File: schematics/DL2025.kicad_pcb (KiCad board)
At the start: 2 copper layers, 95.5 x 45.3 mm, 6 parts, among them U1 ATmega328PB-A, U2 DS18B20, U3 BMP280, U4 SC16IS750xPW, U8 CC56-12GWA, U9 AMS1117-3.3

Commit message: updated PCB schematic
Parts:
- removed U4: SC16IS750xPW, Package_SO:TSSOP-24_4.4x7.8mm_P0.65mm
- added C1: 100n, Capacitor_THT:C_Radial_D4.0mm_H5.0mm_P1.50mm, F.Cu at (132.6, 31.2)
- added C2: 100n, Capacitor_THT:C_Radial_D4.0mm_H5.0mm_P1.50mm, F.Cu at (114.8, 28.4)
- added C3: 100n, Capacitor_THT:C_Radial_D4.0mm_H5.0mm_P1.50mm, F.Cu at (144.9, 57.0)
- added C4: 100n, Capacitor_THT:C_Radial_D4.0mm_H5.0mm_P1.50mm, F.Cu at (113.7, 52.3)
- added C5: 100n, Capacitor_THT:C_Radial_D4.0mm_H5.0mm_P1.50mm, F.Cu at (110.3, 28.4)
- added C6: 100n, Capacitor_THT:C_Radial_D4.0mm_H5.0mm_P1.50mm, F.Cu at (129.8, 40.2)
- added J1: Micro_SD_Card, Connector_PinHeader_1.00mm:PinHeader_1x09_P1.00mm_Horizontal, F.Cu at (149.1, 54.1)
- added R1: 4.7K, Resistor_THT:R_Axial_DIN0207_L6.3mm_D2.5mm_P2.54mm_Vertical, F.Cu at (139.3, 31.0)
- added R2: 4.7K, Resistor_THT:R_Axial_DIN0207_L6.3mm_D2.5mm_P2.54mm_Vertical, F.Cu at (138.7, 25.3)
- added U5: FT232RL, Package_SO:SSOP-28_5.3x10.2mm_P0.65mm, F.Cu at (122.8, 38.8)
- moved U9 0.68 mm to (122.6, 26.2)
- moved U1 0.26 mm to (124.7, 55.3)
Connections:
- U1 pad 4: +5V -> Net-(U1-VCC)
- U3 pad 3: Net-(U1-PC4) -> Net-(U3-SDI)
- U3 pad 4: Net-(U1-PC5) -> Net-(U3-SCK)
- U9 pad 3: +5V -> Net-(U9-VI)
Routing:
- net Net-(U9-VO): track 6.36 -> 134.5 mm, vias 0 -> 1
- net GND: track 147.2 -> 24.3 mm, vias 0 -> 11
- net Net-(J1-DAT3/CD): track 0.00 -> 69.8 mm
- net Net-(U1-PC0): track 109.4 -> 47.3 mm
- net Net-(U1-PE3): track 106.9 -> 52.6 mm
- net Net-(U1-PE2): track 124.4 -> 72.1 mm
- net Net-(J1-DAT0): track 67.2 -> 25.4 mm
- net Net-(J1-CMD): track 0.00 -> 30.5 mm
- net Net-(U1-PE1): track 150.8 -> 123.5 mm
- net Net-(U1-PC1): track 64.0 -> 41.7 mm
- net Net-(J1-CLK): track 0.00 -> 20.6 mm
- net Net-(U1-VCC): track 0.00 -> 10.8 mm
- net Net-(U3-SDI): track 0.00 -> 9.30 mm
- net Net-(U1-PE0): track 116.9 -> 108.1 mm
- net Net-(U1-PB0): track 152.1 -> 143.4 mm
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- added copper zone on B.Cu, net GND
- added copper zone on F.Cu, net GND

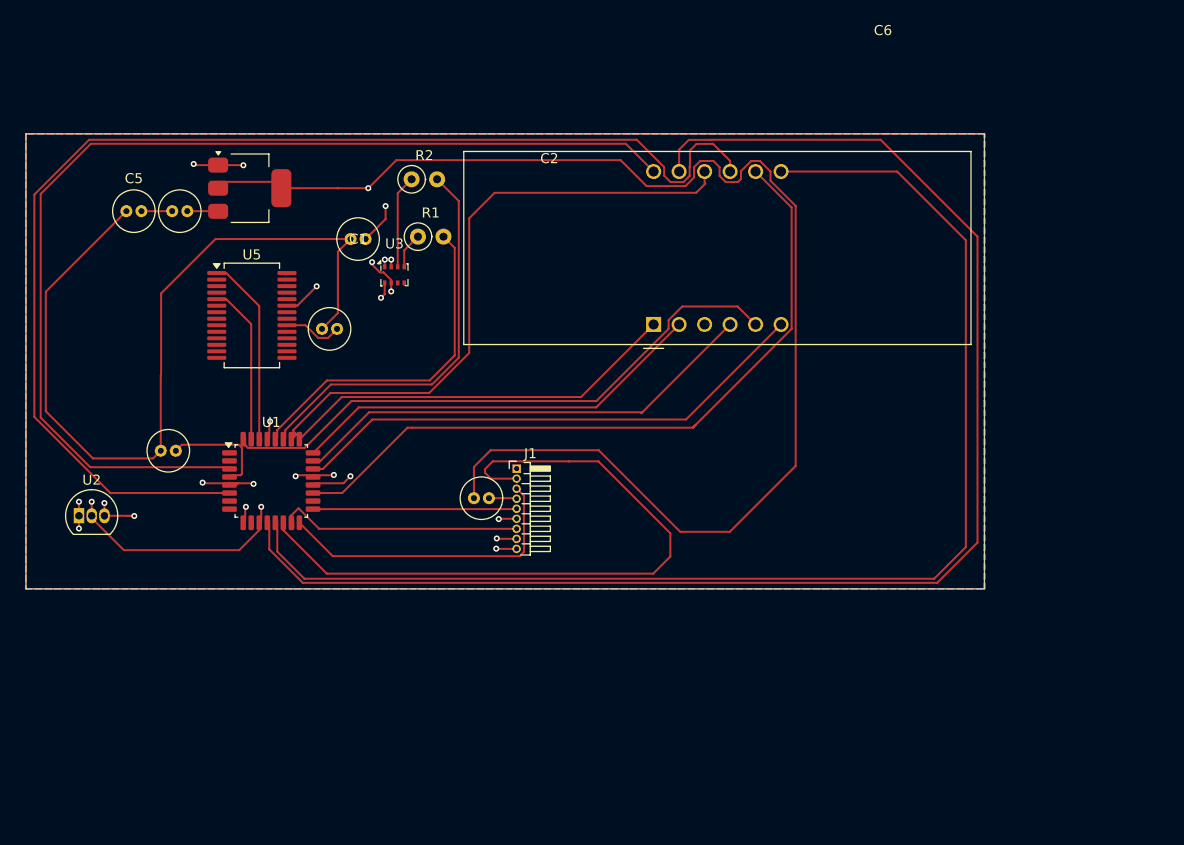
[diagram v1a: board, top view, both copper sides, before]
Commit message: updated schematics
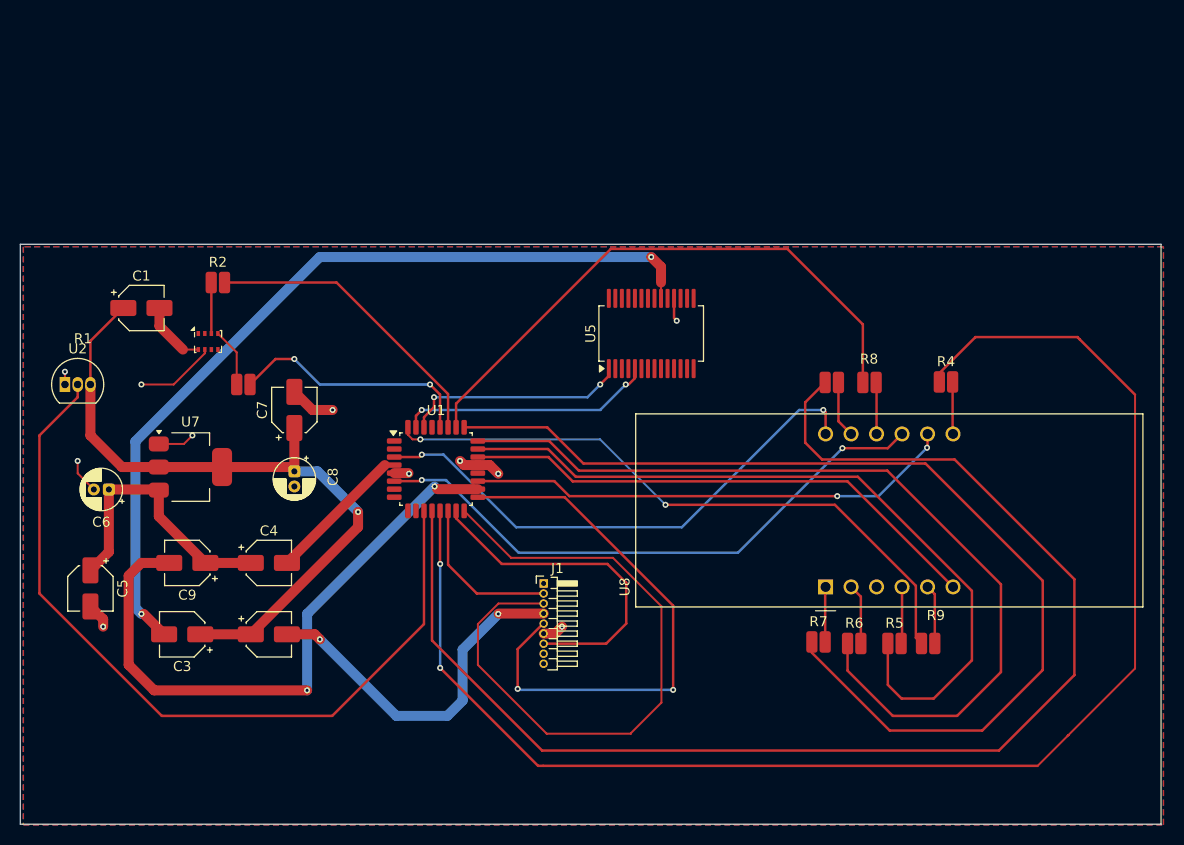
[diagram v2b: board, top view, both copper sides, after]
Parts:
- removed U9: AMS1117-3.3, Package_TO_SOT_SMD:SOT-223-3_TabPin2
- added C7: 100n, Capacitor_SMD:CP_Elec_4x3, F.Cu at (127.0, 48.3)
- added C8: 10u, Capacitor_THT:CP_Radial_D4.0mm_P1.50mm, F.Cu at (127.0, 54.4)
- added C9: 100n, Capacitor_SMD:CP_Elec_4x3, F.Cu at (116.3, 63.5)
- added R3: 220, Resistor_SMD:R_0508_1220Metric_Pad1.12x2.15mm_HandSolder, F.Cu at (180.6, 45.5)
- added R4: 220, Resistor_SMD:R_0508_1220Metric_Pad1.12x2.15mm_HandSolder, F.Cu at (191.9, 45.5)
- added R5: 220, Resistor_SMD:R_0508_1220Metric_Pad1.12x2.15mm_HandSolder, F.Cu at (186.8, 71.5)
- added R6: 220, Resistor_SMD:R_0508_1220Metric_Pad1.12x2.15mm_HandSolder, F.Cu at (182.8, 71.5)
- added R7: 220, Resistor_SMD:R_0508_1220Metric_Pad1.12x2.15mm_HandSolder, F.Cu at (179.2, 71.4)
- added R8: 220, Resistor_SMD:R_0508_1220Metric_Pad1.12x2.15mm_HandSolder, F.Cu at (184.3, 45.5)
- added R9: 220, Resistor_SMD:R_0508_1220Metric_Pad1.12x2.15mm_HandSolder, F.Cu at (190.2, 71.5)
- added U7: AMS1117-3.3, Package_TO_SOT_SMD:SOT-223-3_TabPin2, F.Cu at (116.6, 53.9)
- C1, C2, C3, C4, C5: footprint Capacitor_THT:C_Radial_D4.0mm_H5.0mm_P1.50mm -> Capacitor_SMD:CP_Elec_4x3
- C6: value 100n -> 10u; footprint Capacitor_THT:C_Radial_D4.0mm_H5.0mm_P1.50mm -> Capacitor_THT:CP_Radial_D4.0mm_P1.50mm
- R1, R2: footprint Resistor_THT:R_Axial_DIN0207_L6.3mm_D2.5mm_P2.54mm_Vertical -> Resistor_SMD:R_0508_1220Metric_Pad1.12x2.15mm_HandSolder
- moved C2 43.2 mm to (124.5, 70.6)
- moved U5 39.8 mm to (162.6, 40.6), turned to 90 degrees
- moved C5 37.8 mm to (106.7, 66.0), turned to -90 degrees
- moved C3 32.1 mm to (115.8, 70.6), turned to 180 degrees
- moved U8 31.3 mm to (179.9, 65.9)
- moved C6 26.6 mm to (108.5, 56.2), turned to 180 degrees
- moved R1 22.8 mm to (121.9, 45.7)
- moved C1 21.9 mm to (111.8, 38.1)
- moved R2 21.9 mm to (119.4, 35.6)
- moved U3 19.7 mm to (118.4, 41.4)
- moved U1 16.5 mm to (141.1, 54.1)
- moved C4 15.5 mm to (124.5, 63.5)
- moved U2 13.2 mm to (104.1, 45.7)
- moved J1 11.8 mm to (151.8, 65.5)
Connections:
- C1 pad 1: +5V -> Net-(U2-V_{DD})
- C2 pad 1: Net-(U7-VI) -> Net-(U2-V_{DD})
- C2 pad 2: Net-(U9-VI) -> Net-(J1-VDD)
- C3 pad 1: Net-(U9-VO) -> Net-(U2-V_{DD})
- C3 pad 2: Net-(J1-VDD) -> Net-(U5-VCC)
- C5 pad 2: Net-(U7-VI) -> GND
- C6 pad 2: Net-(U5-VCC) -> GND
- U1 pad 18: unconnected-(U1-AVCC-Pad18) -> Net-(U1-AVCC)
- U8 pad 1: Net-(U1-PC2) -> Net-(U8-e)
- U8 pad 10: Net-(U1-PC3) -> Net-(U8-f)
- U8 pad 11: Net-(U1-PB0) -> Net-(U8-a)
- U8 pad 2: Net-(U1-PC1) -> Net-(U8-d)
- U8 pad 4: Net-(U1-PC0) -> Net-(U8-c)
- U8 pad 5: Net-(U1-PD2) -> Net-(U8-g)
- U8 pad 7: Net-(U1-PB1) -> Net-(U8-b)
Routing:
- net Net-(U9-VO): track 134.5 -> 0.00 mm, vias 1 -> 0
- net Net-(U5-VCC): track 5.89 -> 84.1 mm, vias 0 -> 2
- net Net-(U1-PE1): track 123.5 -> 58.5 mm, vias 0 -> 2
- net Net-(U2-V_{DD}): track 5.26 -> 69.9 mm, vias 2 -> 1
- net Net-(U1-PC2): track 39.8 -> 102.7 mm
- net Net-(U1-AVCC): track 0.00 -> 62.3 mm, vias 0 -> 2
- net Net-(U1-PD7): track 22.6 -> 80.8 mm, vias 2 -> 0
- net +5V: track 83.9 -> 27.6 mm
- net Net-(U1-PE0): track 108.1 -> 53.2 mm, vias 0 -> 2
- net Net-(J1-DAT3/CD): track 69.8 -> 16.1 mm
- net Net-(U1-PC1): track 41.7 -> 88.5 mm
- net Net-(J1-CMD): track 30.5 -> 67.1 mm
- net Net-(J1-CLK): track 20.6 -> 55.5 mm, vias 0 -> 2
- net Net-(J1-VDD): track 2.78 -> 36.1 mm, vias 0 -> 2
- net Net-(U1-PC0): track 47.3 -> 76.7 mm
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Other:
- board size 95.5 x 45.3 mm -> 113.7 x 57.8 mm
